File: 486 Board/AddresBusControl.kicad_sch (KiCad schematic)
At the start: 22 parts, among them U10 74LVC1GU04DRL, U11 74573, U12 74573, U13 74AHC244, U14 74573, U15 74573, U16 74AHC244, U17 74573, U18 74AHC244, U19 74573, U20 74AHC244

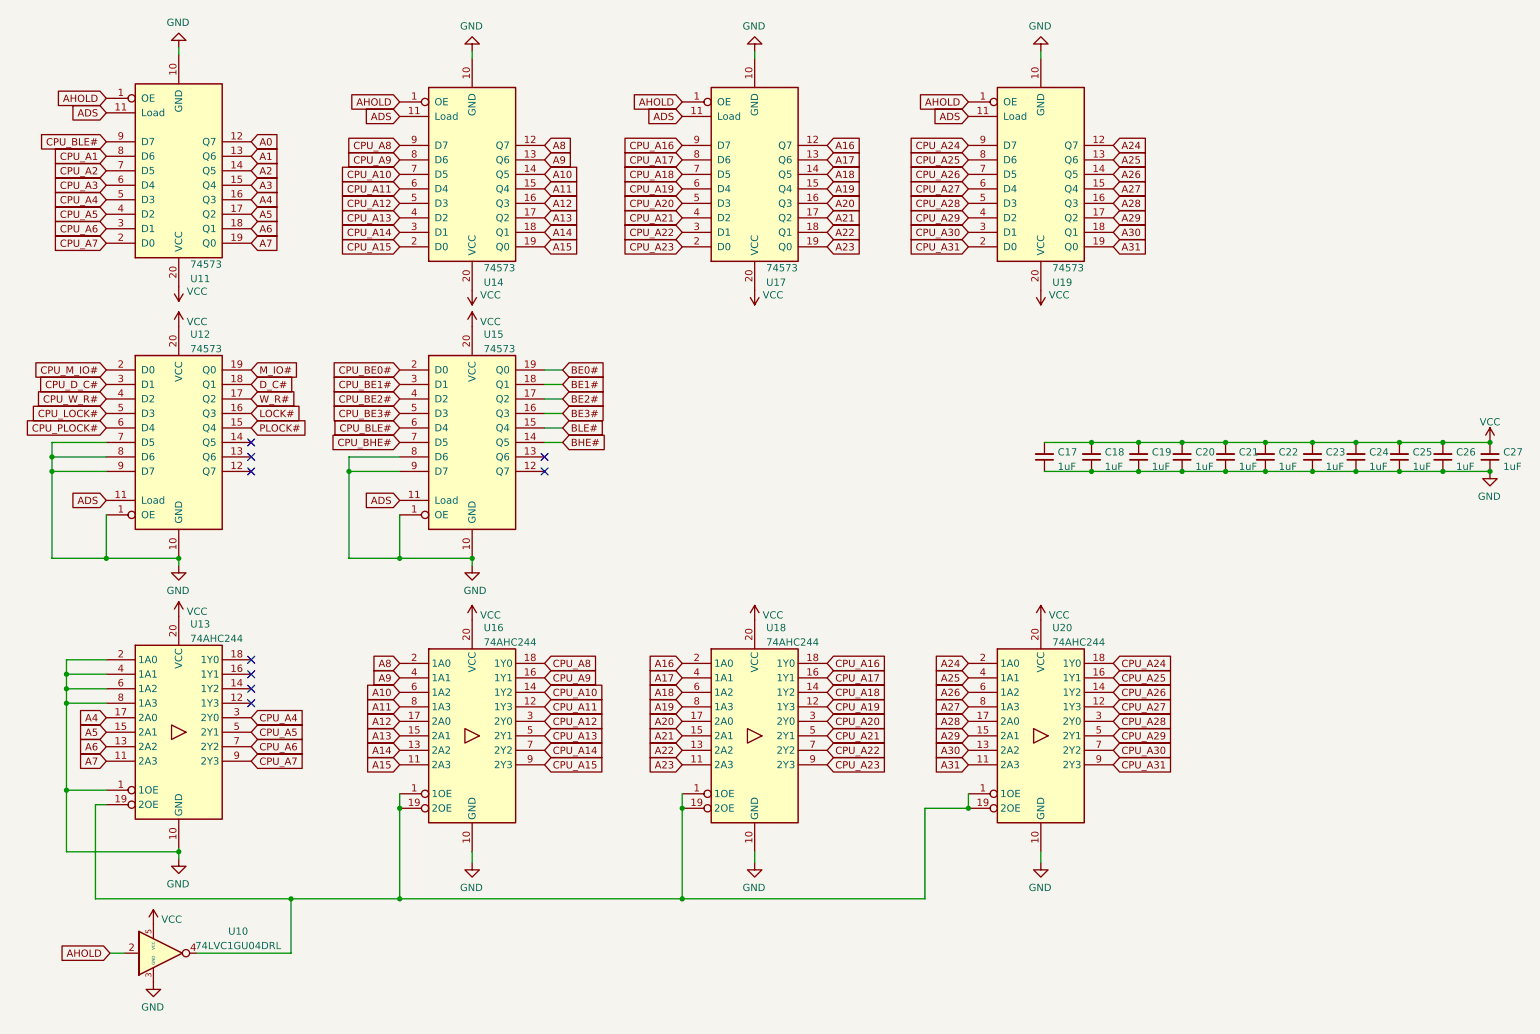
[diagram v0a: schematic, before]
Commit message: * Layout Template for eurocard format * 486 Board updated to new layout * Support board draft * Added 6u eurocard backplane meant for ATX case
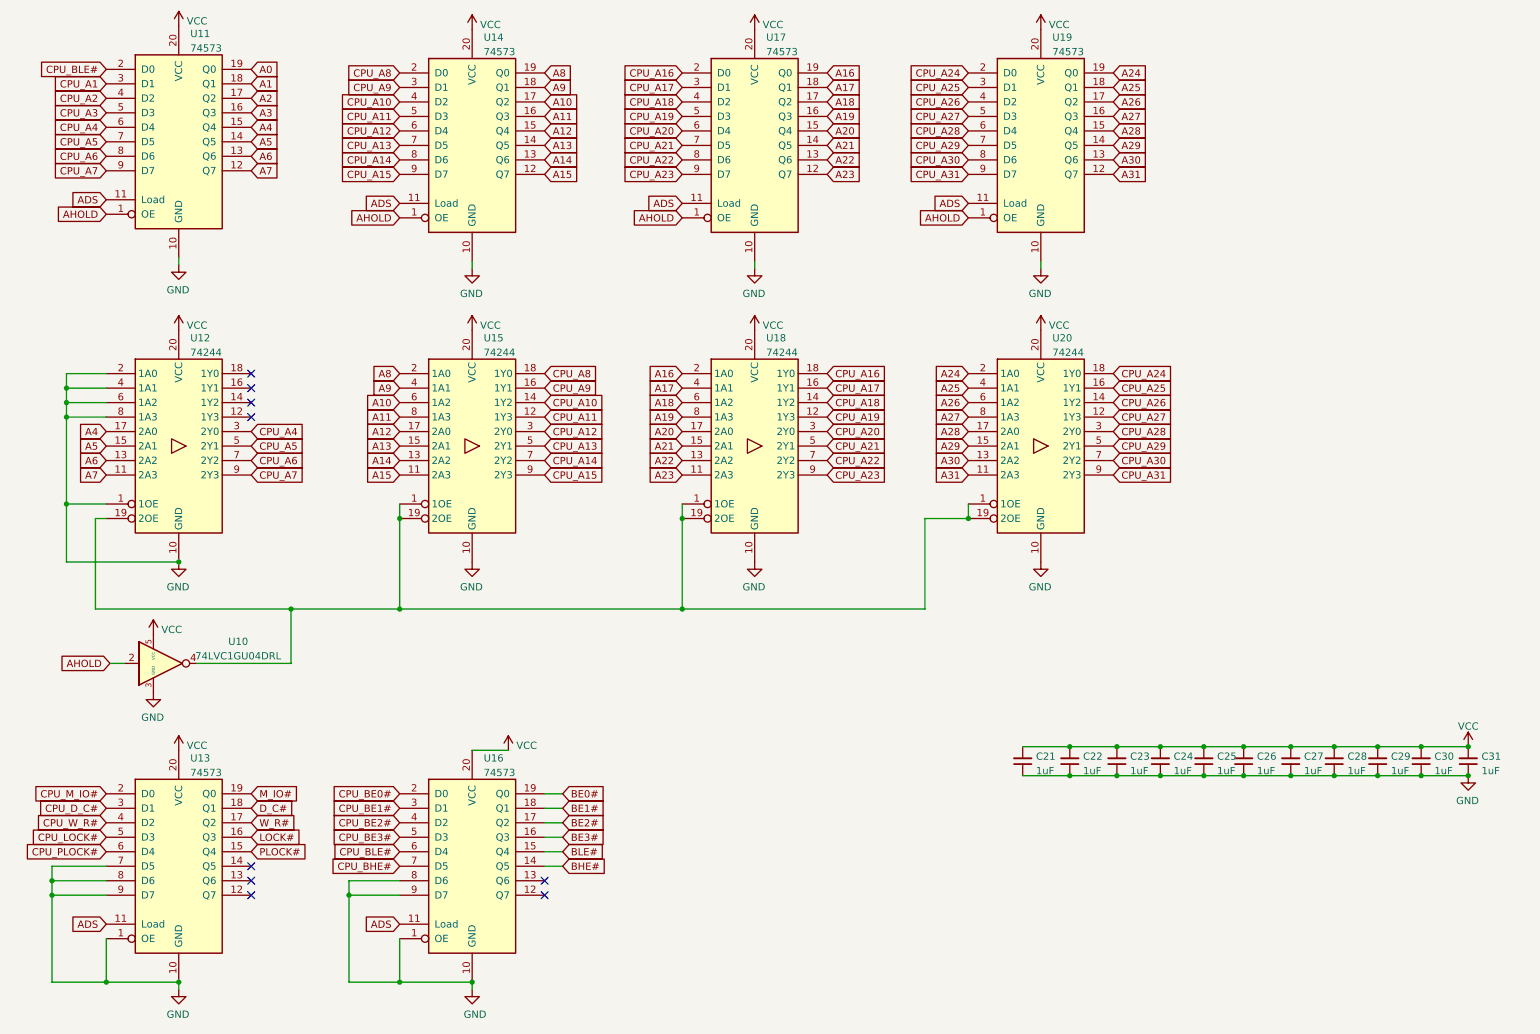
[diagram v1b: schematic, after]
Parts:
- U12: renamed from U13; value 74AHC244 -> 74244
- U15: renamed from U16; value 74AHC244 -> 74244
- U18, U20: value 74AHC244 -> 74244
- renumbered C17 to C21, C18 to C22, C19 to C23, C20 to C24, C21 to C25, C22 to C26, C23 to C27, C24 to C28, C25 to C29, C26 to C30, C27 to C31, U12 to U13, U15 to U16
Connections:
- net A0: now also U11.19 (Q0); no longer U11.12 (Q7)
- net A1: now also U11.18 (Q1); no longer U11.13 (Q6)
- net A10: now also U14.17 (Q2); no longer U14.14 (Q5)
- net A11: now also U14.16 (Q3); no longer U14.15 (Q4)
- net A12: now also U14.15 (Q4); no longer U14.16 (Q3)
- net A13: now also U14.14 (Q5); no longer U14.17 (Q2)
- net A14: now also U14.13 (Q6); no longer U14.18 (Q1)
- net A15: now also U14.12 (Q7); no longer U14.19 (Q0)
- net A16: now also U17.19 (Q0); no longer U17.12 (Q7)
- net A17: now also U17.18 (Q1); no longer U17.13 (Q6)
- net A18: now also U17.17 (Q2); no longer U17.14 (Q5)
- net A19: now also U17.16 (Q3); no longer U17.15 (Q4)
- net A2: now also U11.17 (Q2); no longer U11.14 (Q5)
- net A20: now also U17.15 (Q4); no longer U17.16 (Q3)
- net A21: now also U17.14 (Q5); no longer U17.17 (Q2)
- net A22: now also U17.13 (Q6); no longer U17.18 (Q1)
- net A23: now also U17.12 (Q7); no longer U17.19 (Q0)
- net A24: now also U19.19 (Q0); no longer U19.12 (Q7)
- net A25: now also U19.18 (Q1); no longer U19.13 (Q6)
- net A26: now also U19.17 (Q2); no longer U19.14 (Q5)
- net A27: now also U19.16 (Q3); no longer U19.15 (Q4)
- net A28: now also U19.15 (Q4); no longer U19.16 (Q3)
- net A29: now also U19.14 (Q5); no longer U19.17 (Q2)
- net A3: now also U11.16 (Q3); no longer U11.15 (Q4)
- net A30: now also U19.13 (Q6); no longer U19.18 (Q1)
- net A31: now also U19.12 (Q7); no longer U19.19 (Q0)
- net A4: now also U11.15 (Q4); no longer U11.16 (Q3)
- net A5: now also U11.14 (Q5); no longer U11.17 (Q2)
- net A6: now also U11.13 (Q6); no longer U11.18 (Q1)
- net A7: now also U11.12 (Q7); no longer U11.19 (Q0)
- net A8: now also U14.19 (Q0); no longer U14.12 (Q7)
- net A9: now also U14.18 (Q1); no longer U14.13 (Q6)
- net CPU_A1: now also U11.3 (D1); no longer U11.8 (D6)
- net CPU_A10: now also U14.4 (D2); no longer U14.7 (D5)
- net CPU_A11: now also U14.5 (D3); no longer U14.6 (D4)
- net CPU_A12: now also U14.6 (D4); no longer U14.5 (D3)
- net CPU_A13: now also U14.7 (D5); no longer U14.4 (D2)
- net CPU_A14: now also U14.8 (D6); no longer U14.3 (D1)
- net CPU_A15: now also U14.9 (D7); no longer U14.2 (D0)
- net CPU_A16: now also U17.2 (D0); no longer U17.9 (D7)
- net CPU_A17: now also U17.3 (D1); no longer U17.8 (D6)
- net CPU_A18: now also U17.4 (D2); no longer U17.7 (D5)
- net CPU_A19: now also U17.5 (D3); no longer U17.6 (D4)
- net CPU_A2: now also U11.4 (D2); no longer U11.7 (D5)
- net CPU_A20: now also U17.6 (D4); no longer U17.5 (D3)
- net CPU_A21: now also U17.7 (D5); no longer U17.4 (D2)
- net CPU_A22: now also U17.8 (D6); no longer U17.3 (D1)
- net CPU_A23: now also U17.9 (D7); no longer U17.2 (D0)
- net CPU_A24: now also U19.2 (D0); no longer U19.9 (D7)
- net CPU_A25: now also U19.3 (D1); no longer U19.8 (D6)
- net CPU_A26: now also U19.4 (D2); no longer U19.7 (D5)
- net CPU_A27: now also U19.5 (D3); no longer U19.6 (D4)
- net CPU_A28: now also U19.6 (D4); no longer U19.5 (D3)
- net CPU_A29: now also U19.7 (D5); no longer U19.4 (D2)
- net CPU_A3: now also U11.5 (D3); no longer U11.6 (D4)
- net CPU_A30: now also U19.8 (D6); no longer U19.3 (D1)
- net CPU_A31: now also U19.9 (D7); no longer U19.2 (D0)
- net CPU_A4: now also U11.6 (D4); no longer U11.5 (D3)
- net CPU_A5: now also U11.7 (D5); no longer U11.4 (D2)
- net CPU_A6: now also U11.8 (D6); no longer U11.3 (D1)
- net CPU_A7: now also U11.9 (D7); no longer U11.2 (D0)
- net CPU_A8: now also U14.2 (D0); no longer U14.9 (D7)
- net CPU_A9: now also U14.3 (D1); no longer U14.8 (D6)
- net CPU_BLE#: now also U11.2 (D0); no longer U11.9 (D7)
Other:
- moved on the sheet: C21, C22, C23, C24, C25, C26, C27, C28, C29, C30, C31, U10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
